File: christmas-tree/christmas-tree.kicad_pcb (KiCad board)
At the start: 2 copper layers, 66 x 93.5 mm, 65 parts, among them J1 USB_C_Receptacle_USB2.0, J2 CORTEX_DEBUG_ETM, J3 CONN_01X03, M1 MECHANICAL, U1 NCP45525IMNTWG-H, U10 19-C47/RSGHBHC-5V01/2T, U11 19-C47/RSGHBHC-5V01/2T, U12 ZLDO1117-33, U2 74LVC1T45, U3 19-C47/RSGHBHC-5V01/2T, U4 19-C47/RSGHBHC-5V01/2T, U5 19-C47/RSGHBHC-5V01/2T, U6 19-C47/RSGHBHC-5V01/2T, U7 19-C47/RSGHBHC-5V01/2T, U8 19-C47/RSGHBHC-5V01/2T, U9 STM32L031-QFN32

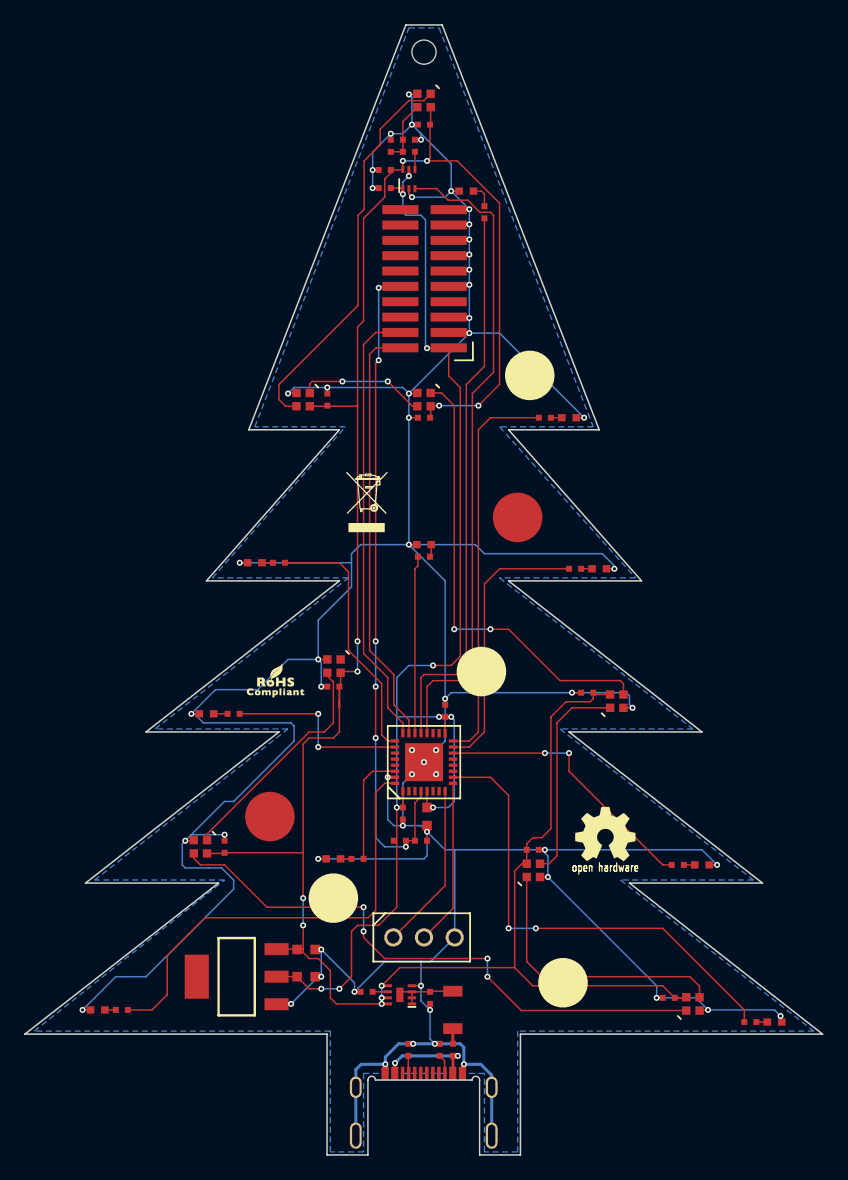
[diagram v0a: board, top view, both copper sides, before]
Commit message: Switch to larger vias for cheap fab
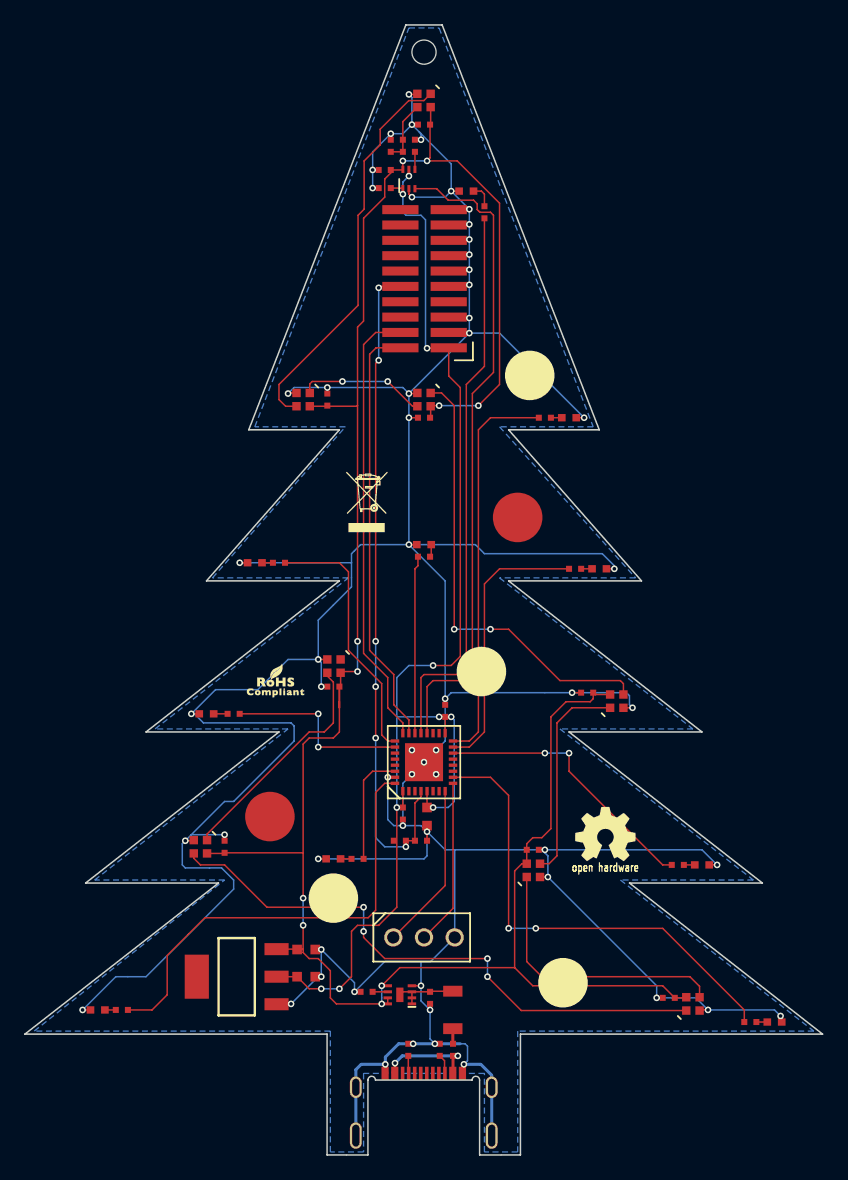
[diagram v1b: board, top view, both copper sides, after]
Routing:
- net /5V0: vias 11 -> 10
